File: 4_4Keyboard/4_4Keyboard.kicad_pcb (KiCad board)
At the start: 2 copper layers, 64 parts, among them J1 USB_B_Mini, J2 Conn_01x06, J3 Conn_02x07_Counter_Clockwise, SW1 DOOM KEY, U1 STM32L476RCTx, U2 LD1117S33CTR

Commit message: Board layout first push
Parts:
- removed D18, D24: 1N5819, Diode_THT:D_DO-41_SOD81_P10.16mm_Horizontal
- added D6: LED, LED_THT:LED_D5.0mm, F.Cu at (106.3, 35.9)
- added LED0_R1: LED0_R, Resistor_THT:R_Axial_DIN0207_L6.3mm_D2.5mm_P7.62mm_Horizontal, F.Cu at (99.9, 31.1)
- added LED1_R1: LED1_R, Resistor_THT:R_Axial_DIN0207_L6.3mm_D2.5mm_P7.62mm_Horizontal, F.Cu at (48.4, 41.1)
- added LED2_R1: LED2_R, Resistor_THT:R_Axial_DIN0207_L6.3mm_D2.5mm_P7.62mm_Horizontal, F.Cu at (48.4, 47.8)
- added LED3_R1: LED3_R, Resistor_THT:R_Axial_DIN0207_L6.3mm_D2.5mm_P7.62mm_Horizontal, F.Cu at (48.4, 54.4)
- added LED4_R1: LED4_R, Resistor_THT:R_Axial_DIN0207_L6.3mm_D2.5mm_P7.62mm_Horizontal, F.Cu at (48.5, 61.0)
- added R2_C2: 1N5819, Diode_THT:D_DO-41_SOD81_P10.16mm_Horizontal, F.Cu at (200.4, 118.5)
- added R3_C3: 1N5819, Diode_THT:D_DO-41_SOD81_P10.16mm_Horizontal, F.Cu at (220.0, 138.3)
- FB1: value Ferrite_Bead 600 -> Ferrite Bead
- J2: value Conn_01x06 -> SERIAL WIRE
- J3: value Conn_02x07_Counter_Clockwise -> Pin Breakout
- KEY_SWITCH1: value SW_Push -> R0_C0
- KEY_SWITCH10: value SW_Push -> R4_C1
- KEY_SWITCH11: value SW_Push -> R0_C2
- KEY_SWITCH12: value SW_Push -> R1_C2
- KEY_SWITCH13: value SW_Push -> R2_C2
- KEY_SWITCH14: value SW_Push -> R3_C2
- KEY_SWITCH15: value SW_Push -> R4_C2
- KEY_SWITCH16: value SW_Push -> R0_C3
- KEY_SWITCH17: value SW_Push -> R1_C3
- KEY_SWITCH18: value SW_Push -> R2_C3
- KEY_SWITCH19: value SW_Push -> R3_C3
- KEY_SWITCH2: value SW_Push -> R1_C0
- KEY_SWITCH20: value SW_Push -> R4_C3
- KEY_SWITCH3: value SW_Push -> R2_C0
- KEY_SWITCH4: value SW_Push -> R3_C0
- KEY_SWITCH5: value SW_Push -> R4_C0
- KEY_SWITCH6: value SW_Push -> R0_C1
- KEY_SWITCH7: value SW_Push -> R1_C1
- KEY_SWITCH8: value SW_Push -> R2_C1
- KEY_SWITCH9: value SW_Push -> R3_C1
- moved KEY_SWITCH20 183.1 mm to (228.0, 143.5)
- moved KEY_SWITCH19 165.6 mm to (228.0, 123.8)
- moved KEY_SWITCH18 165.3 mm to (228.0, 104.1)
- moved KEY_SWITCH15 149.9 mm to (208.3, 143.5)
- moved D4 148.1 mm to (41.1, 61.0)
- moved KEY_SWITCH17 145.4 mm to (228.0, 84.5)
- moved D2 143.3 mm to (41.1, 47.8)
- moved C1 137.7 mm to (64.1, 59.9)
- moved D5 135.2 mm to (66.4, 32.0)
- moved R0_C1 133.0 mm to (180.3, 79.4)
- moved D3 132.3 mm to (41.1, 54.4)
- moved D1 132.0 mm to (41.1, 41.1)
- moved KEY_SWITCH7 131.6 mm to (188.6, 84.5)
- moved KEY_SWITCH14 130.8 mm to (208.3, 123.8)
- moved KEY_SWITCH11 129.3 mm to (208.3, 64.8)
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- renumbered D6 to R0_C0, D11 to R0_C1, D16 to R0_C2, D21 to R0_C3, D7 to R1_C0, D12 to R1_C1, D17 to R1_C2, D22 to R1_C3, D8 to R2_C0, D13 to R2_C1, D23 to R2_C3, D9 to R3_C0, D14 to R3_C1, D19 to R3_C2, D10 to R4_C0, D15 to R4_C1, D20 to R4_C2, D25 to R4_C3, SW1 to RESET1
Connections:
- C5 pad 1: Net-(C5-Pad1) -> GND
- C5 pad 2: Net-(C5-Pad2) -> /VCC_3_3
- D5 pad 1: /FS_DP -> /FS_DM
- D5 pad 3: /FS_DM -> /FS_DP
- J3 pad 10: /D_PIN_8 -> /D_PIN_11
- J3 pad 11: /D_PIN_9 -> /D_PIN_10
- J3 pad 12: /D_PIN_10 -> /D_PIN_9
- J3 pad 13: /D_PIN_11 -> /D_PIN_8
- J3 pad 14: /D_PIN_12 -> /D_PIN_7
- J3 pad 9: /D_PIN_7 -> /D_PIN_12
- U1 pad 56: Net-(D1-Pad2) -> Net-(LED1_R1-Pad2)
- U1 pad 57: Net-(D2-Pad2) -> Net-(LED2_R1-Pad2)
- U1 pad 58: Net-(D3-Pad2) -> Net-(LED3_R1-Pad2)
- U1 pad 59: Net-(D4-Pad2) -> Net-(LED4_R1-Pad2)
- U1 pad 64: Net-(C5-Pad2) -> /VCC_3_3

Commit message: Board Design Start
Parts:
- added J4: Conn_01x07, Connector_PinHeader_2.54mm:PinHeader_1x07_P2.54mm_Vertical, F.Cu at (116.5, 45.5)
- J3: value Pin Breakout -> Conn_01x07; footprint Connector_PinHeader_2.54mm:PinHeader_2x07_P2.54mm_Vertical -> Connector_PinHeader_2.54mm:PinHeader_1x07_P2.54mm_Vertical
- moved R1_C0 117.9 mm to (44.1, 111.8)
- moved R3_C2 117.9 mm to (83.1, 150.5)
- moved R4_C3 117.9 mm to (102.6, 170.4)
- moved KEY_SWITCH1 117.9 mm to (51.7, 77.0)
- moved KEY_SWITCH10 117.9 mm to (71.4, 155.7)
- moved KEY_SWITCH11 117.9 mm to (91.1, 77.0)
- moved KEY_SWITCH12 117.9 mm to (91.1, 96.6)
- moved KEY_SWITCH13 117.9 mm to (91.1, 116.3)
- moved KEY_SWITCH14 117.9 mm to (91.1, 136.0)
- moved KEY_SWITCH15 117.9 mm to (91.1, 155.7)
- moved KEY_SWITCH16 117.9 mm to (110.7, 77.0)
- moved KEY_SWITCH17 117.9 mm to (110.7, 96.6)
- moved KEY_SWITCH18 117.9 mm to (110.7, 116.3)
- moved KEY_SWITCH19 117.9 mm to (110.7, 136.0)
- moved KEY_SWITCH2 117.9 mm to (51.7, 96.6)
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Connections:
- J3 pad 1: /D_PIN_1 -> GND
- J3 pad 2: /D_PIN_2 -> /D_PIN_3
- J3 pad 3: /D_PIN_3 -> /D_PIN_5
- J3 pad 4: /D_PIN_4 -> /D_PIN_7
- J3 pad 5: /D_PIN_5 -> /D_PIN_9
- J3 pad 6: /D_PIN_6 -> /D_PIN_11
- J3 pad 7: /VCC_3_3 -> /D_PIN_13
- U1 pad 17: /D_PIN_6 -> /D_PIN_10
- U1 pad 20: /D_PIN_5 -> /D_PIN_12
- U1 pad 21: /D_PIN_4 -> /D_PIN_14
- U1 pad 22: /D_PIN_3 -> /D_PIN_13
- U1 pad 23: /D_PIN_2 -> /D_PIN_11
- U1 pad 24: /D_PIN_1 -> /D_PIN_9
- U1 pad 25: /D_PIN_12 -> /D_PIN_7
- U1 pad 26: /D_PIN_7 -> /D_PIN_5
- U1 pad 27: /D_PIN_8 -> /D_PIN_3
- U1 pad 28: /D_PIN_9 -> /D_PIN_4
- U1 pad 29: /D_PIN_10 -> /D_PIN_6
- U1 pad 30: /D_PIN_11 -> /D_PIN_8
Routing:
- net /COL_2: track 0.00 -> 306.8 mm
- net /COL_3: track 0.00 -> 165.2 mm
- net /COL_1: track 0.00 -> 146.7 mm
- net /ROW_1: track 0.00 -> 117.8 mm, vias 0 -> 2
- net /ROW_0: track 0.00 -> 87.5 mm
- net /COL_0: track 0.00 -> 83.5 mm
- net /D_PIN_8: track 0.00 -> 63.1 mm
- net /D_PIN_6: track 0.00 -> 59.7 mm
- net /ROW_4: track 0.00 -> 59.1 mm
- net /ROW_3: track 0.00 -> 59.1 mm
- net /ROW_2: track 0.00 -> 59.1 mm
- net /D_PIN_10: track 0.00 -> 53.5 mm
- net /D_PIN_12: track 0.00 -> 50.5 mm
- net /D_PIN_14: track 0.00 -> 45.8 mm
- net /D_PIN_13: track 0.00 -> 42.5 mm
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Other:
- board outline added: 109.7 x 175.9 mm
- net class Power added: clearance 0.2, trace_width 0.25, via_dia 0.7, via_drill 0.5

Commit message: Trace ripup
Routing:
- net /COL_2: track 306.8 -> 0.00 mm
- net /COL_3: track 165.2 -> 0.00 mm
- net /COL_1: track 146.7 -> 0.00 mm
- net /ROW_1: track 117.8 -> 0.00 mm, vias 2 -> 0
- net /ROW_0: track 87.5 -> 0.04 mm
- net /COL_0: track 83.5 -> 0.00 mm
- net /ROW_4: track 59.1 -> 0.00 mm
- net /ROW_3: track 59.1 -> 0.00 mm
- net /ROW_2: track 59.1 -> 0.00 mm
- net Net-(KEY_SWITCH2-Pad2): track 16.3 -> 0.00 mm
- net Net-(KEY_SWITCH3-Pad2): track 16.3 -> 0.00 mm
- net Net-(KEY_SWITCH7-Pad2): track 16.0 -> 0.00 mm
- net Net-(KEY_SWITCH17-Pad2): track 16.0 -> 0.00 mm
- net Net-(KEY_SWITCH9-Pad2): track 16.0 -> 0.00 mm
- net Net-(KEY_SWITCH4-Pad2): track 16.0 -> 0.00 mm
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
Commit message: Autorouting prep
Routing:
- net /D_PIN_8: track 63.1 -> 0.00 mm
- net /D_PIN_6: track 59.7 -> 0.00 mm
- net /D_PIN_10: track 53.5 -> 0.00 mm
- net /D_PIN_12: track 50.5 -> 0.00 mm
- net /D_PIN_14: track 45.8 -> 0.00 mm
- net /D_PIN_13: track 42.5 -> 0.00 mm
- net /D_PIN_4: track 41.9 -> 0.00 mm
- net /D_PIN_11: track 41.6 -> 0.00 mm
- net /D_PIN_9: track 40.8 -> 0.00 mm
- net /D_PIN_7: track 39.9 -> 0.00 mm
- net /D_PIN_5: track 39.1 -> 0.00 mm
- net /D_PIN_3: track 38.6 -> 0.00 mm
- net Net-(J1-Pad1): track 20.6 -> 0.00 mm
- net Net-(LED4_R1-Pad2): track 15.2 -> 0.00 mm
- net Net-(LED1_R1-Pad2): track 14.5 -> 0.00 mm
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
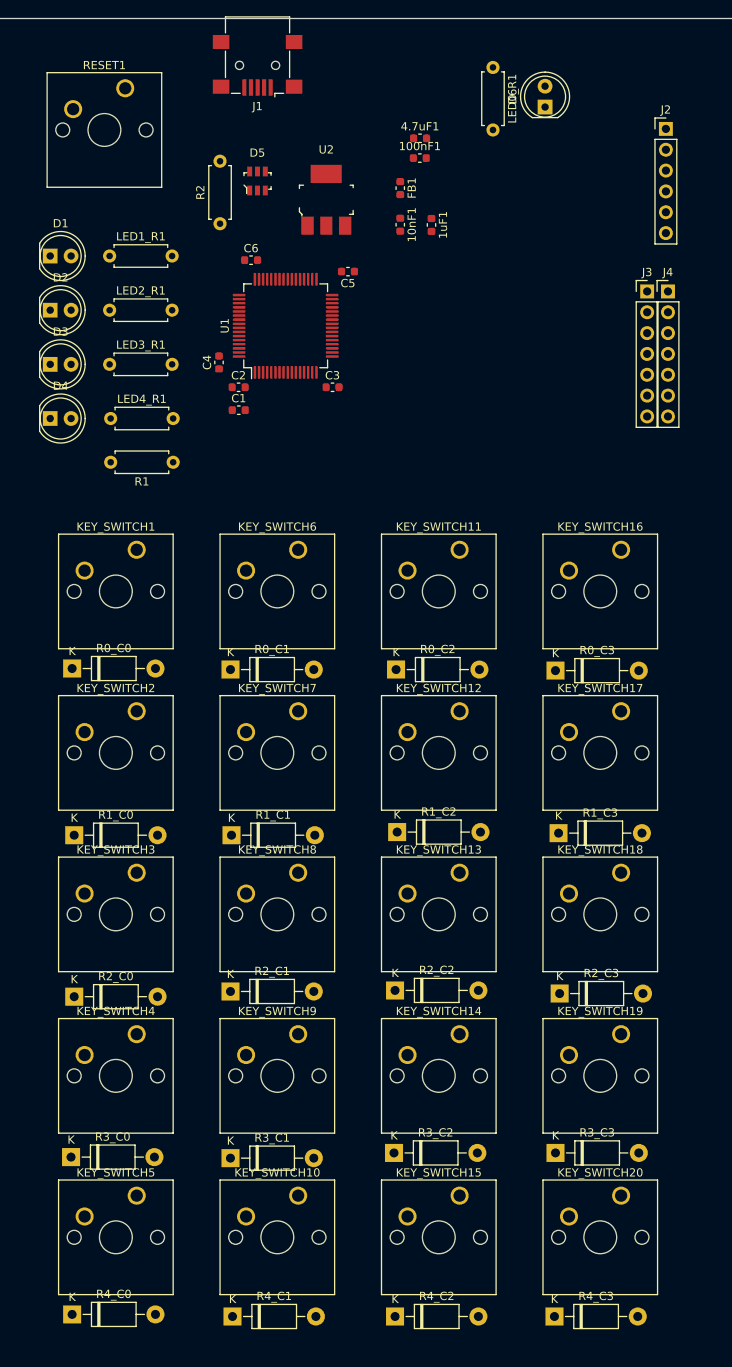
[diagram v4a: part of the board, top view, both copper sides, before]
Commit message: Autorouting complete
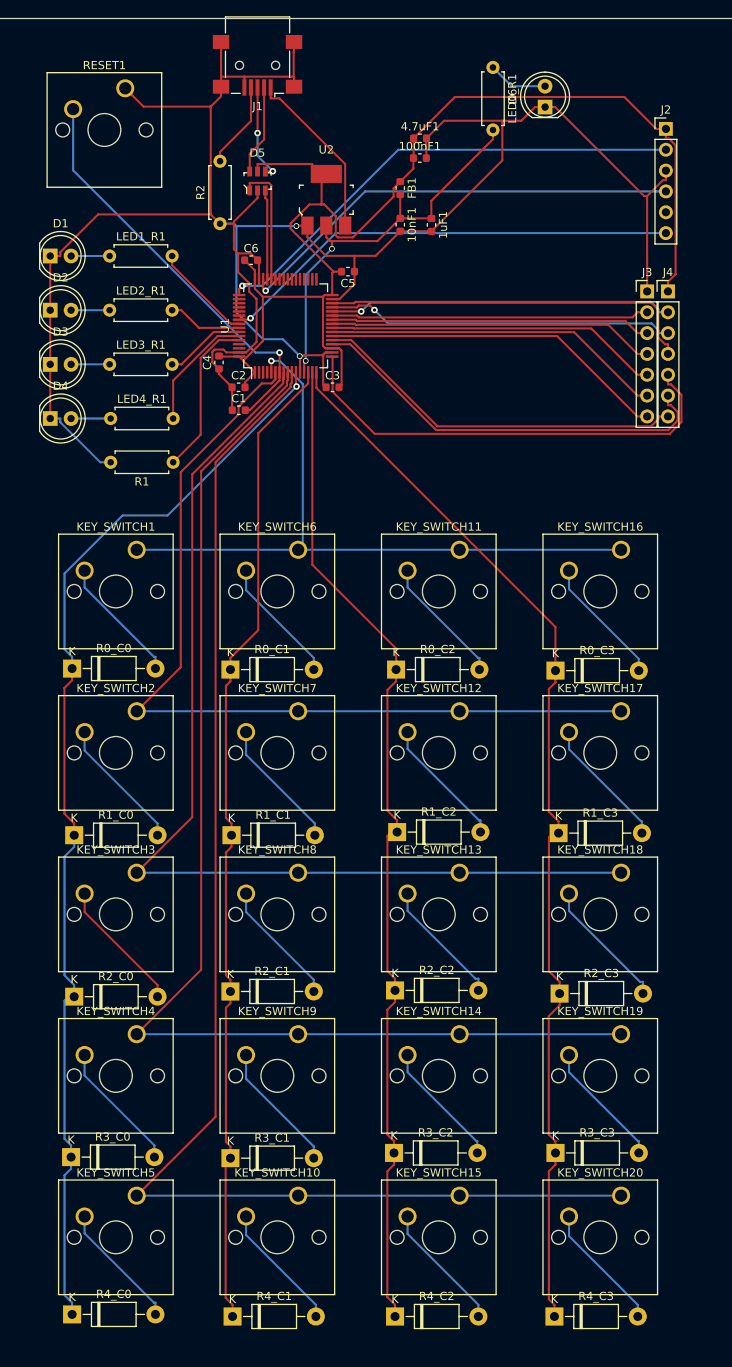
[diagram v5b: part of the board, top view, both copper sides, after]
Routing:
- net GND: track 0.00 -> 279.2 mm, vias 0 -> 2
- net /ROW_4: track 0.00 -> 167.3 mm
- net /VCC_3_3: track 0.00 -> 150.9 mm
- net /ROW_3: track 0.00 -> 147.4 mm
- net /COL_0: track 0.00 -> 134.3 mm, vias 0 -> 1
- net /COL_3: track 0.00 -> 131.3 mm
- net /ROW_2: track 0.00 -> 127.5 mm
- net /COL_2: track 0.00 -> 123.3 mm
- net /COL_1: track 0.00 -> 121.7 mm
- net /ROW_1: track 0.00 -> 108.1 mm
- net /ROW_0: track 0.00 -> 85.7 mm, vias 0 -> 1
- net /SWCLK: track 0.00 -> 59.8 mm, vias 0 -> 1
- net /TRACESWO: track 0.00 -> 56.4 mm, vias 0 -> 1
- net /D_PIN_10: track 0.00 -> 56.2 mm
- net /SWDIO: track 0.00 -> 55.3 mm, vias 0 -> 1
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
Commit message: First Version Done
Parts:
- added G***: LOGO, 4_4Keyboard:pj_logo, B.Cu at (64.5, 151.8)
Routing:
- net GND: track 279.2 -> 237.4 mm
- added copper zone on B.Cu, net GND

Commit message: Final Push
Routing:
- net GND: track 237.4 -> 274.0 mm
- net /D_PIN_8: track 46.3 -> 43.9 mm, vias 0 -> 1
- net Net-(C1-Pad2): track 50.9 -> 49.2 mm
- net /D_PIN_6: track 42.6 -> 43.9 mm, vias 1 -> 0
- net /VCC_3_3: track 150.9 -> 151.5 mm
- net /COL_1: track 121.7 -> 121.1 mm
- added copper zone on F.Cu, net GND
